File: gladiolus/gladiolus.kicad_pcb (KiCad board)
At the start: 4 copper layers, 70.7 x 53.3 mm, 138 parts, among them J1 NEIGHBOR1, J2 NEIGHBOR2, J3 Conn_01x02_Female, J7 BONUS_ROW, Q1 Q_NPN_BEC, U1 THS4520RGT, U2 AD8330ARQZ, U3 AD9283, U4 AD9704, U5 LMH6643, U6 74LVC1G3157, U7 74LVC1G3157

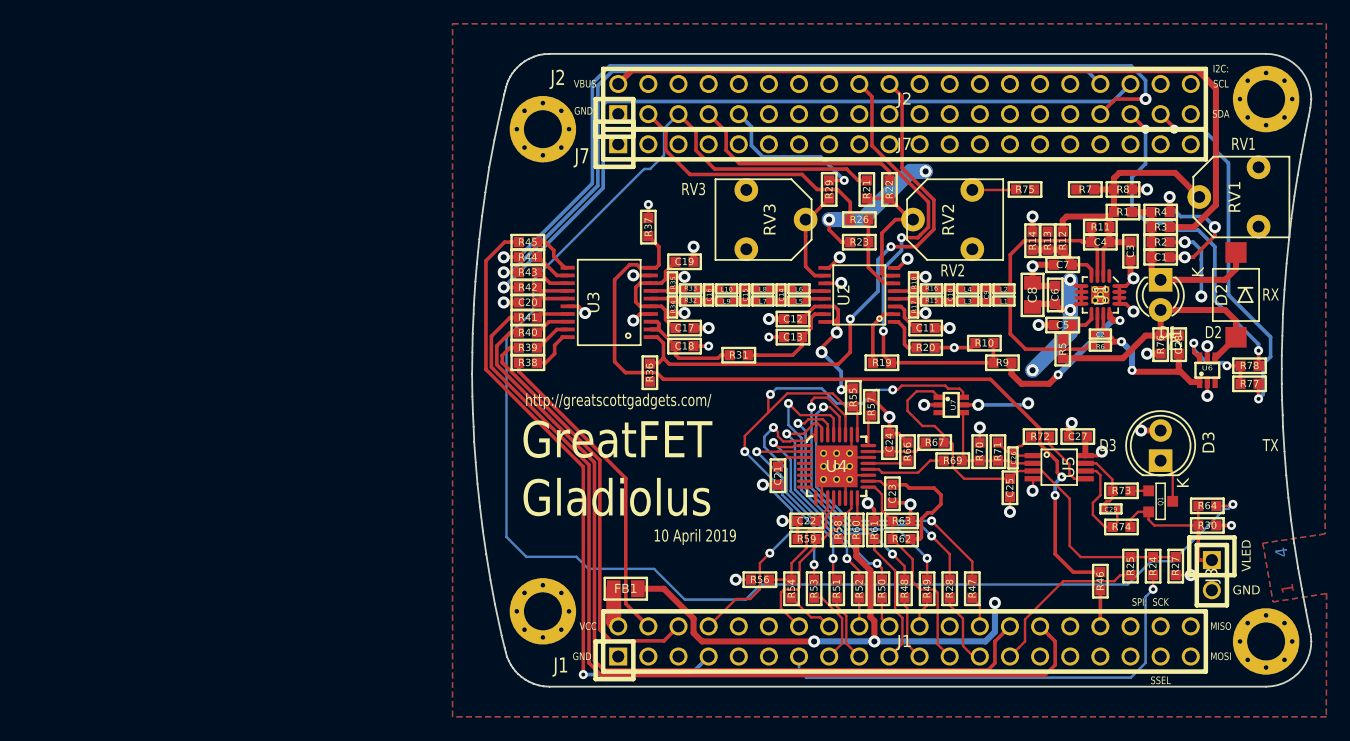
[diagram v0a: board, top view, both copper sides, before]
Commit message: Gladiolus: Added test points, switched connections on RV1, moved TX shutoff switch position, changed RX switch control pin from SPIFI pin J2.37
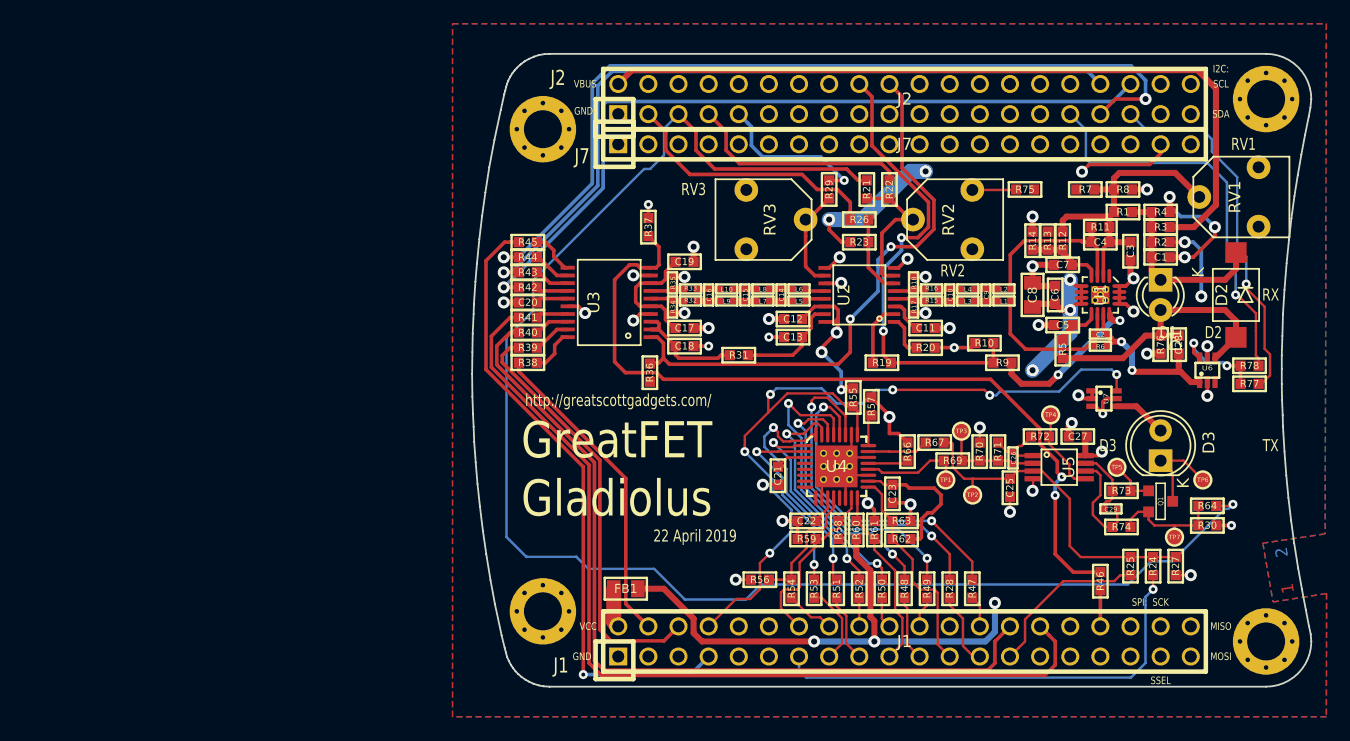
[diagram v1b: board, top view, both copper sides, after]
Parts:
- removed C24: 100nF, gsg-modules:0603
- removed J3: Conn_01x02_Female, gsg-modules:HEADER-1x2
- added TP1: TestPoint, gsg-modules:TESTPOINT-50MIL, F.Cu at (149.5, 104.5)
- added TP2: TestPoint, gsg-modules:TESTPOINT-50MIL, F.Cu at (151.8, 105.8)
- added TP3: TestPoint, gsg-modules:TESTPOINT-50MIL, F.Cu at (150.9, 100.4)
- added TP4: TestPoint, gsg-modules:TESTPOINT-50MIL, F.Cu at (158.4, 99.0)
- added TP5: TestPoint, gsg-modules:TESTPOINT-50MIL, F.Cu at (164.0, 103.4)
- added TP6: TestPoint, gsg-modules:TESTPOINT-50MIL, F.Cu at (171.2, 104.5)
- added TP7: TestPoint, gsg-modules:TESTPOINT-50MIL, F.Cu at (168.8, 109.3)
- moved U7 12.9 mm to (162.9, 97.6)
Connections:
- D3 pad 2: VCC -> Net-(D3-Pad2)
- J2 pad 31: (no net) -> /P6_7
- J2 pad 37: /P3_5 -> (no net)
- R77 pad 2: /P3_5 -> /P2_1
- R78 pad 1: /P2_1 -> /P6_7
- RV1 pad 1: GND -> VCC
- RV1 pad 3: VCC -> GND
- U7 pad 1: Net-(C25-Pad1) -> GND
- U7 pad 3: (no net) -> VCC
- U7 pad 4: Net-(C26-Pad1) -> Net-(D3-Pad2)
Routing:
- net /P6_7: track 0.00 -> 33.9 mm, vias 0 -> 1
- net /P3_5: track 30.9 -> 0.00 mm, vias 2 -> 0
- net /P5_0: track 54.7 -> 69.5 mm, vias 4 -> 6
- net GND: track 89.2 -> 97.8 mm, vias 43 -> 44
- net Net-(C25-Pad1): track 36.2 -> 28.9 mm
- net Net-(D3-Pad2): track 0.00 -> 4.62 mm
- net /TXOUT: track 3.85 -> 8.08 mm
- net VCC: track 139.4 -> 135.5 mm, vias 18 -> 16
- net Net-(Q1-Pad2): track 13.1 -> 10.1 mm
- net Net-(Q1-Pad1): track 1.52 -> 3.98 mm
- net Net-(R72-Pad2): track 5.36 -> 7.24 mm
- net Net-(R69-Pad2): track 6.89 -> 8.59 mm
- net Net-(C26-Pad1): track 10.3 -> 8.83 mm
- net /P2_1: track 29.8 -> 31.0 mm, vias 2 -> 1
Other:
- board text added: "22 April 2019"
- board text removed: "10 April 2019"
- board text removed: "4"
- board text removed: "VLED"

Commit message: Changed TX switch control to J1_24 and the ADC clock to J2_P6
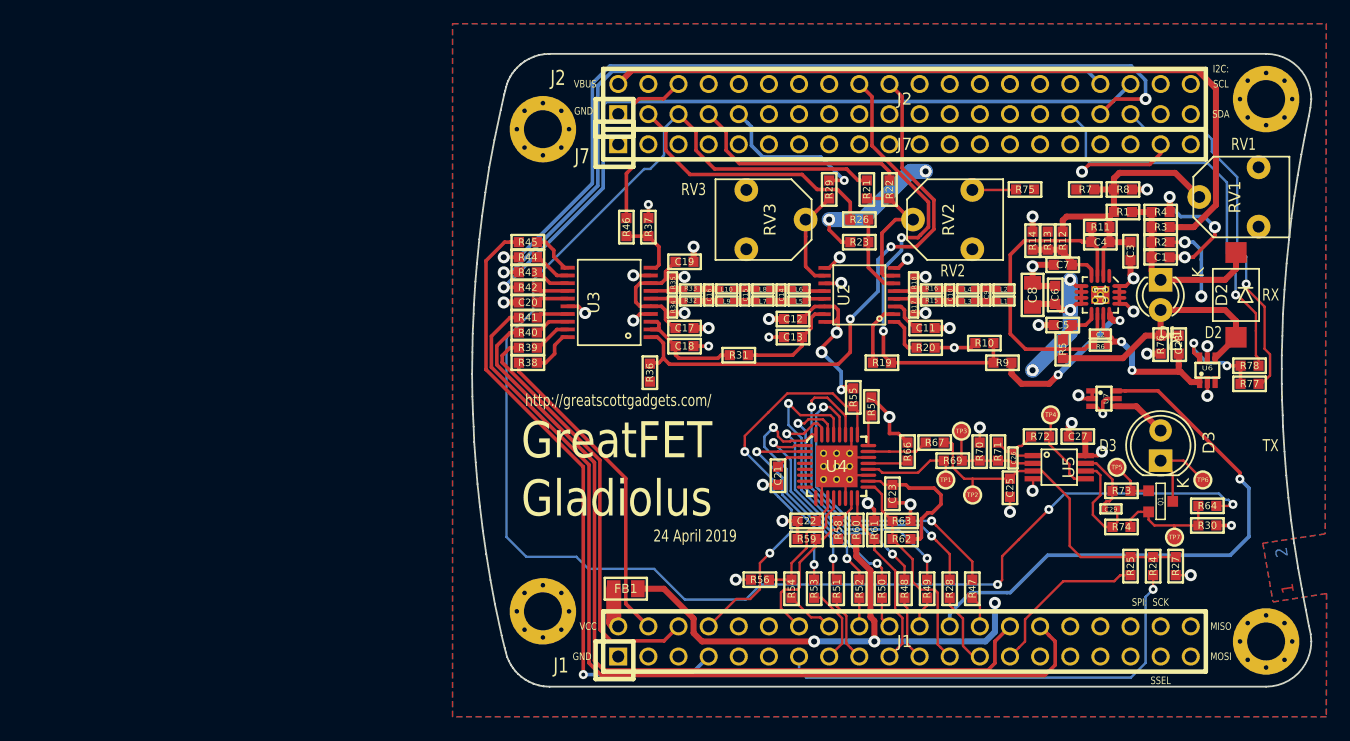
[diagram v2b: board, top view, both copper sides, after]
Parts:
- moved R46 49.9 mm to (122.6, 83.2), turned to 90 degrees
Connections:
- J1 pad 24: (no net) -> /P5_4
- J1 pad 34: /P9_6 -> (no net)
- J2 pad 6: (no net) -> /P4_5
- R46 pad 2: /P9_6 -> /P4_5
- U7 pad 6: /P5_0 -> /P5_4
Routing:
- net /ADCCLK: track 68.4 -> 5.43 mm, vias 2 -> 0
- net /P5_4: track 0.00 -> 48.0 mm, vias 0 -> 1
- net /P5_0: track 69.5 -> 34.9 mm, vias 6 -> 2
- net /P4_5: track 0.00 -> 14.3 mm
- net /P9_6: track 3.05 -> 0.00 mm
- net /ADC0_0: track 129.3 -> 131.2 mm, vias 1 -> 3
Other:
- board text added: "24 April 2019"
- board text removed: "22 April 2019"

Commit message: Gladiolus: Added EEPROM and changed to default DAC control for second RX gain stage
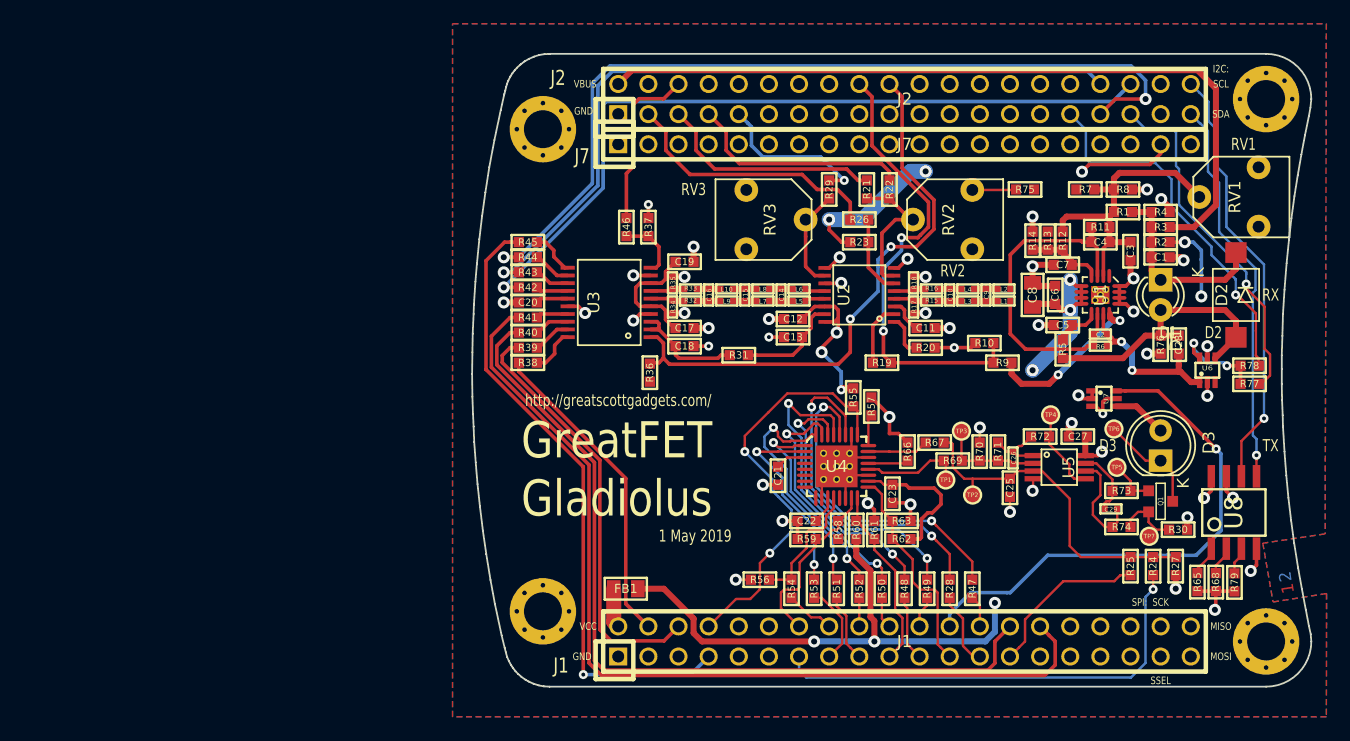
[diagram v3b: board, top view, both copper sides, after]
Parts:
- removed R64: 0, gsg-modules:0603
- added R65: 1k, gsg-modules:0603, F.Cu at (170.7, 113.1)
- added R68: 1k, gsg-modules:0603, F.Cu at (172.3, 113.1)
- added R79: 1k, gsg-modules:0603, F.Cu at (173.9, 113.1)
- added U8: AT34C02D, gsg-modules:SOIC8-154, F.Cu at (173.8, 107.2)
- moved TP6 8.64 mm to (163.7, 100.2)
- moved R30 2.49 mm to (169.1, 108.7)
- moved TP7 2.13 mm to (166.7, 109.2)
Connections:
- J2 pad 39: (no net) -> /I2C0_SDA
- J2 pad 40: (no net) -> /I2C0_SCL
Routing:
- net /ADC0_0: track 131.2 -> 19.1 mm, vias 3 -> 0
- net /I2C0_SCL: track 0.00 -> 36.4 mm, vias 0 -> 1
- net /I2C0_SDA: track 0.00 -> 33.0 mm, vias 0 -> 1
- net VCC: track 135.5 -> 142.4 mm, vias 16 -> 18
- net GND: track 97.8 -> 92.4 mm, vias 44 -> 45
- net Net-(Q1-Pad2): track 10.1 -> 6.09 mm
- net /P5_4: track 48.0 -> 44.4 mm
- net Net-(R65-Pad2): track 0.00 -> 3.05 mm
- net /P6_7: track 33.9 -> 31.3 mm
- net Net-(R68-Pad2): track 0.00 -> 2.54 mm
- net Net-(R79-Pad2): track 0.00 -> 2.32 mm
- net /P2_1: track 31.0 -> 29.5 mm
- net /TXOUT: track 8.08 -> 8.89 mm
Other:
- copper layers 4 -> 2
- board text added: "1 May 2019"
- board text removed: "24 April 2019"
- board text removed: "3"
